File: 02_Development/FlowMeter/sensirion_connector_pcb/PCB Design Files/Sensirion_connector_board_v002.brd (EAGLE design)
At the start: 19 x 18.7 mm, 11 parts, among them J1 ED8199-04-ND, J2 277-2419-ND, U1 P82B715TD

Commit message: Added power jumper, redid all manufacturing files & BOMs
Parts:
- J2: value 277-2419-ND -> 277-2419-ND + 277-2418-ND
- moved C1 430.1 mm to (15.8, 13.7)
- moved C2 430.1 mm to (15.8, 11.7)
- moved J1 430.1 mm to (5.69, 15.2)
- moved J2 430.1 mm to (4.47, 6.70)
- moved JP10 430.1 mm to (3.28, 11.0)
- moved JP11 430.1 mm to (14.8, 11.1)
- moved R1 430.1 mm to (3.40, 13.7)
- moved R2 430.1 mm to (3.40, 11.9)
- moved R3 430.1 mm to (3.40, 9.37)
- moved R4 430.1 mm to (15.7, 9.37)
- moved U1 430.1 mm to (9.50, 11.3)
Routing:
- net LY: track 14.1 -> 26.4 mm, vias 0 -> 1
- net SCL0: track 28.7 -> 24.6 mm
- net GND: track 6.45 -> 9.78 mm, vias 1 -> 2
- net SDA0: track 47.5 -> 45.6 mm
- net +5V: track 39.1 -> 40.7 mm
- net LX: track 32.1 -> 30.7 mm
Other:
- board text added: "Sensirion Connector PCB 11JAN2021"
- board text added: "©2021 TETRA BIO DISTRIBUTED"
- board text removed: "Sensirio n Connector PCB 12/31/2020"
- board text removed: "Sensirion Connector"

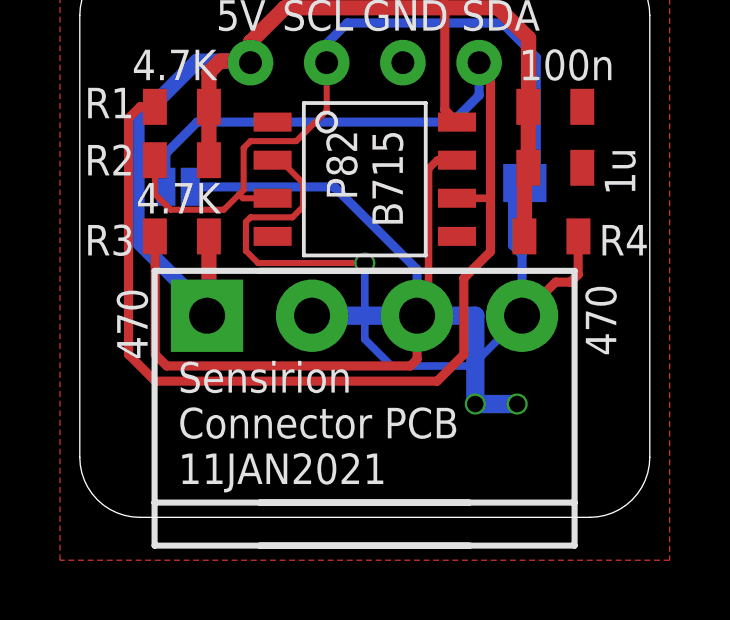
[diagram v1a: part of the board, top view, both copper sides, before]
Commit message: Fixed ground track, updated date & gerbers
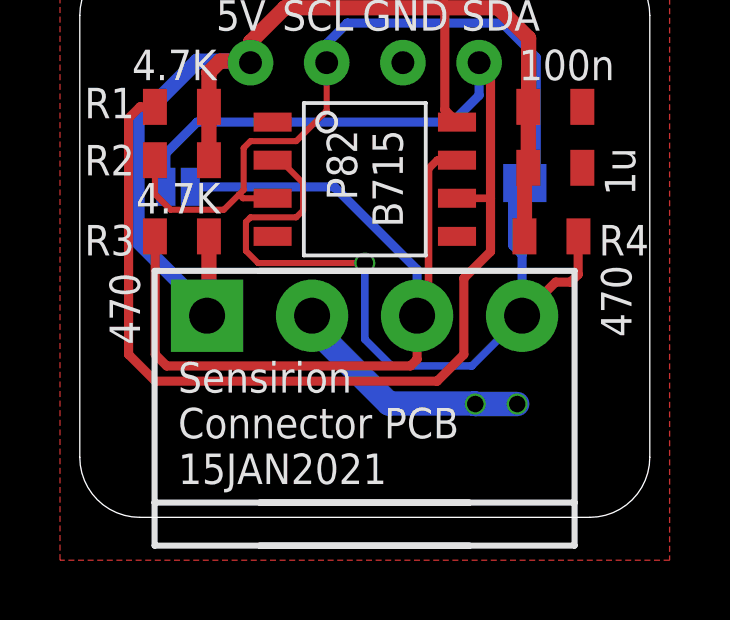
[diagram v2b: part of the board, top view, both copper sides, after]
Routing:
- net GND: track 9.78 -> 8.27 mm
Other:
- board text added: "Sensirion Connector PCB 15JAN2021"
- board text removed: "Sensirion Connector PCB 11JAN2021"
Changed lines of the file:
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@@
 <setting verticaltext="up"/>
 </settings>
-<grid distance="31.25" unitdist="mm" unit="mm" style="lines" multiple="1" display="no" altdistance="5" altunitdist="mil" altunit="mil"/>
+<grid distance="0.005" unitdist="inch" unit="inch" style="lines" multiple="1" display="no" altdistance="5" altunitdist="mil" altunit="mil"/>
 <layers>
 <layer number="1" name="Top" color="4" fill="1" visible="yes" active="yes"/>
@@
 <text x="3.277" y="1.11" size="1.016" layer="21" font="vector" ratio="15">Sensirion
 Connector PCB
-11JAN2021</text>
+15JAN2021</text>
 <text x="14.326" y="16.223" size="0.889" layer="22" font="vector" ratio="15" distance="20" rot="MR0">©2021 TETRA BIO
  DISTRIBUTED</text>
@@
 <attribute name="NAME" x="0.991" y="8.73" size="1.016" layer="21" font="vector" ratio="15" align="bottom-center"/>
 <attribute name="PROD_ID" value="RES-11622" x="4.674" y="9.365" size="1.016" layer="27" font="vector" ratio="15" display="off"/>
-<attribute name="VALUE" x="1.245" y="6.444" size="1.016" layer="21" font="vector" ratio="15" rot="R90" align="top-center"/>
+<attribute name="VALUE" x="0.991" y="6.952" size="1.016" layer="21" font="vector" ratio="15" rot="R90" align="top-center"/>
 </element>
 <element name="R4" library="SparkFun-Resistors" package="0805" value="470" x="15.723" y="9.365" smashed="yes" rot="R180">
 <attribute name="NAME" x="18.136" y="9.746" size="1.016" layer="21" font="vector" ratio="15" rot="R180" align="bottom-center"/>
 <attribute name="PROD_ID" value="RES-11622" x="14.453" y="9.365" size="1.016" layer="27" font="vector" ratio="15" rot="R180" display="off"/>
-<attribute name="VALUE" x="17.882" y="6.571" size="1.016" layer="21" font="vector" ratio="15" rot="R270" align="top-center"/>
+<attribute name="VALUE" x="18.39" y="7.206" size="1.016" layer="21" font="vector" ratio="15" rot="R270" align="top-center"/>
 </element>
 <element name="C1" library="SparkFun-Capacitors" package="0805" value="100n" x="15.85" y="13.683" smashed="yes">
@@
 </polygon>
 <via x="13.183" y="3.777" extent="1-16" drill="0.55"/>
-<wire x1="13.183" y1="3.777" x2="13.183" y2="6.721" width="0.6096" layer="16"/>
-<wire x1="7.7428" y1="6.721" x2="13.183" y2="6.721" width="0.6096" layer="16"/>
 <via x="14.58" y="3.777" extent="1-16" drill="0.55"/>
-<wire x1="13.183" y1="3.777" x2="14.58" y2="3.777" width="0.6096" layer="16"/>
+<wire x1="13.183" y1="3.777" x2="14.58" y2="3.777" width="0.8128" layer="16"/>
+<wire x1="7.7428" y1="6.721" x2="7.7428" y2="6.3542" width="0.8128" layer="16"/>
+<wire x1="7.7428" y1="6.3542" x2="10.30185625" y2="3.79514375" width="0.8128" layer="16"/>
+<wire x1="13.16485625" y1="3.79514375" x2="13.183" y2="3.777" width="0.8128" layer="16"/>
+<wire x1="13.16485625" y1="3.79514375" x2="10.30185625" y2="3.79514375" width="0.8128" layer="16"/>
 </signal>
 <signal name="SCL0">
@@
 <wire x1="7.4426" y1="11.143" x2="6.6806" y2="11.905" width="0.2032" layer="1"/>
 <wire x1="6.4266" y1="11.905" x2="6.6806" y2="11.905" width="0.2032" layer="1"/>
-<wire x1="7.4426" y1="11.143" x2="7.4426" y2="10.3556" width="0.2032" layer="1"/>
-<wire x1="7.4426" y1="10.3556" x2="7.087" y2="10" width="0.2032" layer="1"/>
-<wire x1="7.087" y1="10" x2="5.69" y2="10" width="0.2032" layer="1"/>
+<wire x1="7.4426" y1="11.143" x2="7.4426" y2="10.2286" width="0.2032" layer="1"/>
+<wire x1="7.4426" y1="10.2286" x2="7.214" y2="10" width="0.2032" layer="1"/>
+<wire x1="7.214" y1="10" x2="5.69" y2="10" width="0.2032" layer="1"/>
 <wire x1="5.69" y1="10" x2="5.5376" y2="9.8476" width="0.2032" layer="1"/>
 <wire x1="5.5376" y1="9.8476" x2="5.5376" y2="8.8824" width="0.2032" layer="1"/>

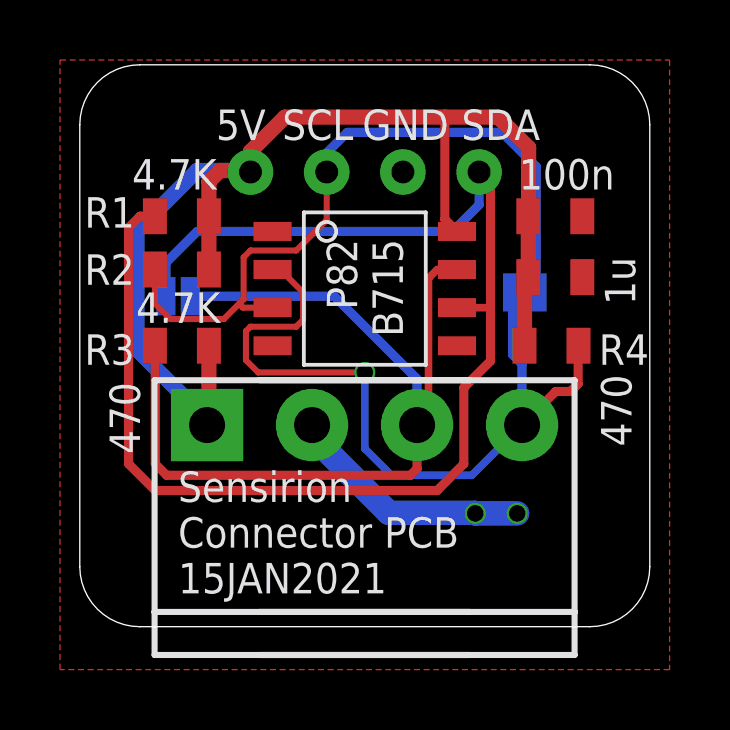
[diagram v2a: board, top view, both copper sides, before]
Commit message: Adjusted board outline to be 20mm x 20mm for JLC Assembly
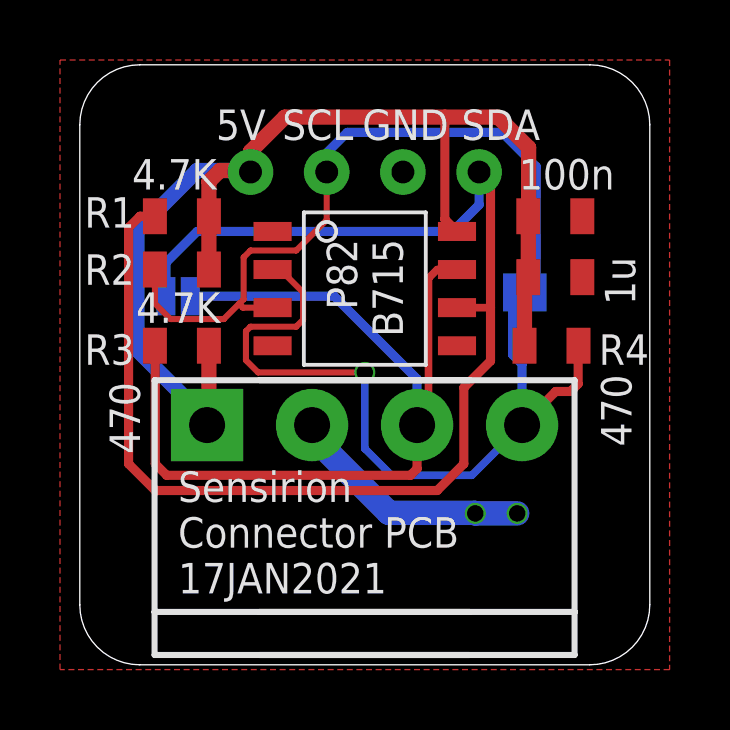
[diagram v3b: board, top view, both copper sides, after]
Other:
- board size 19 x 18.7 mm -> 19 x 20 mm
- board text added: "Sensirion Connector PCB 17JAN2021"
- board text removed: "Sensirion Connector PCB 15JAN2021"
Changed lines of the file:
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@@
 <setting verticaltext="up"/>
 </settings>
-<grid distance="0.005" unitdist="inch" unit="inch" style="lines" multiple="1" display="no" altdistance="5" altunitdist="mil" altunit="mil"/>
+<grid distance="1" unitdist="mm" unit="mm" style="lines" multiple="1" display="no" altdistance="5" altunitdist="mil" altunit="mil"/>
 <layers>
 <layer number="1" name="Top" color="4" fill="1" visible="yes" active="yes"/>
@@
 <board>
 <plain>
-<wire x1="17" y1="0" x2="19" y2="2" width="0.001" layer="20" curve="90"/>
-<wire x1="19" y1="2" x2="19" y2="16.73" width="0.001" layer="20"/>
+<wire x1="0" y1="16.73" x2="0" y2="0.73" width="0.001" layer="20"/>
+<wire x1="0" y1="0.73" x2="2" y2="-1.27" width="0.001" layer="20" curve="90"/>
+<wire x1="2" y1="-1.27" x2="17" y2="-1.27" width="0.001" layer="20"/>
+<wire x1="17" y1="-1.27" x2="19" y2="0.73" width="0.001" layer="20" curve="90"/>
+<wire x1="19" y1="0.73" x2="19" y2="16.73" width="0.001" layer="20"/>
 <wire x1="19" y1="16.73" x2="17" y2="18.73" width="0.001" layer="20" curve="90"/>
 <wire x1="17" y1="18.73" x2="2" y2="18.73" width="0.001" layer="20"/>
 <wire x1="2" y1="18.73" x2="0" y2="16.73" width="0.001" layer="20" curve="90"/>
-<wire x1="0" y1="16.73" x2="0" y2="2" width="0.001" layer="20"/>
-<wire x1="0" y1="2" x2="2" y2="0" width="0.001" layer="20" curve="90"/>
-<wire x1="2" y1="0" x2="17" y2="0" width="0.001" layer="20"/>
 <text x="12.294" y="17.239" size="1.016" layer="21" font="vector" ratio="15" rot="R180">GND</text>
 <text x="15.342" y="17.239" size="1.016" layer="21" font="vector" ratio="15" rot="R180">SDA</text>
@@
 <text x="3.277" y="1.11" size="1.016" layer="21" font="vector" ratio="15">Sensirion
 Connector PCB
-15JAN2021</text>
+17JAN2021</text>
 <text x="14.326" y="16.223" size="0.889" layer="22" font="vector" ratio="15" distance="20" rot="MR0">©2021 TETRA BIO
  DISTRIBUTED</text>

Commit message: Adjusted width of PCB to be 20mm
was still 19mm
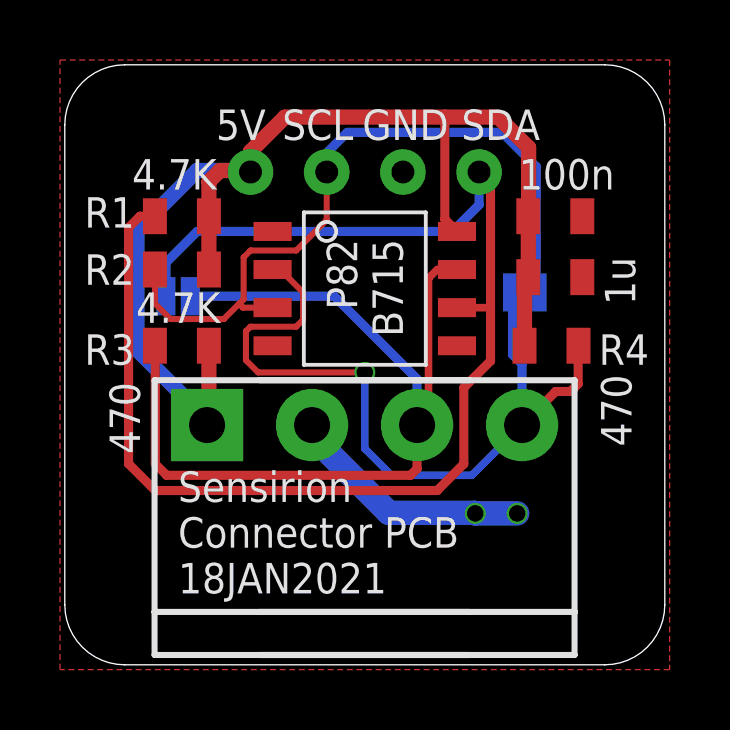
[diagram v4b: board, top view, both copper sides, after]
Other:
- board size 19 x 20 mm -> 20 x 20 mm
- board text added: "Sensirion Connector PCB 18JAN2021"
- board text removed: "Sensirion Connector PCB 17JAN2021"
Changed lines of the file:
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@@
 <board>
 <plain>
-<wire x1="0" y1="16.73" x2="0" y2="0.73" width="0.001" layer="20"/>
-<wire x1="0" y1="0.73" x2="2" y2="-1.27" width="0.001" layer="20" curve="90"/>
-<wire x1="2" y1="-1.27" x2="17" y2="-1.27" width="0.001" layer="20"/>
-<wire x1="17" y1="-1.27" x2="19" y2="0.73" width="0.001" layer="20" curve="90"/>
-<wire x1="19" y1="0.73" x2="19" y2="16.73" width="0.001" layer="20"/>
-<wire x1="19" y1="16.73" x2="17" y2="18.73" width="0.001" layer="20" curve="90"/>
-<wire x1="17" y1="18.73" x2="2" y2="18.73" width="0.001" layer="20"/>
-<wire x1="2" y1="18.73" x2="0" y2="16.73" width="0.001" layer="20" curve="90"/>
+<wire x1="-0.5" y1="16.73" x2="-0.5" y2="0.73" width="0.001" layer="20"/>
+<wire x1="-0.5" y1="0.73" x2="1.5" y2="-1.27" width="0.001" layer="20" curve="90"/>
+<wire x1="1.5" y1="-1.27" x2="17.5" y2="-1.27" width="0.001" layer="20"/>
+<wire x1="17.5" y1="-1.27" x2="19.5" y2="0.73" width="0.001" layer="20" curve="90"/>
+<wire x1="19.5" y1="0.73" x2="19.5" y2="16.73" width="0.001" layer="20"/>
+<wire x1="19.5" y1="16.73" x2="17.5" y2="18.73" width="0.001" layer="20" curve="90"/>
+<wire x1="17.5" y1="18.73" x2="1.5" y2="18.73" width="0.001" layer="20"/>
+<wire x1="1.5" y1="18.73" x2="-0.5" y2="16.73" width="0.001" layer="20" curve="90"/>
 <text x="12.294" y="17.239" size="1.016" layer="21" font="vector" ratio="15" rot="R180">GND</text>
 <text x="15.342" y="17.239" size="1.016" layer="21" font="vector" ratio="15" rot="R180">SDA</text>
@@
 <text x="3.277" y="1.11" size="1.016" layer="21" font="vector" ratio="15">Sensirion
 Connector PCB
-17JAN2021</text>
+18JAN2021</text>
 <text x="14.326" y="16.223" size="0.889" layer="22" font="vector" ratio="15" distance="20" rot="MR0">©2021 TETRA BIO
  DISTRIBUTED</text>
